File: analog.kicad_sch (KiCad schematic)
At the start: 62 parts, among them J8 Sensor harness, J9 Spare diff in, U6 ADS1115 (0x48), U7 ADS1115 (0x49)

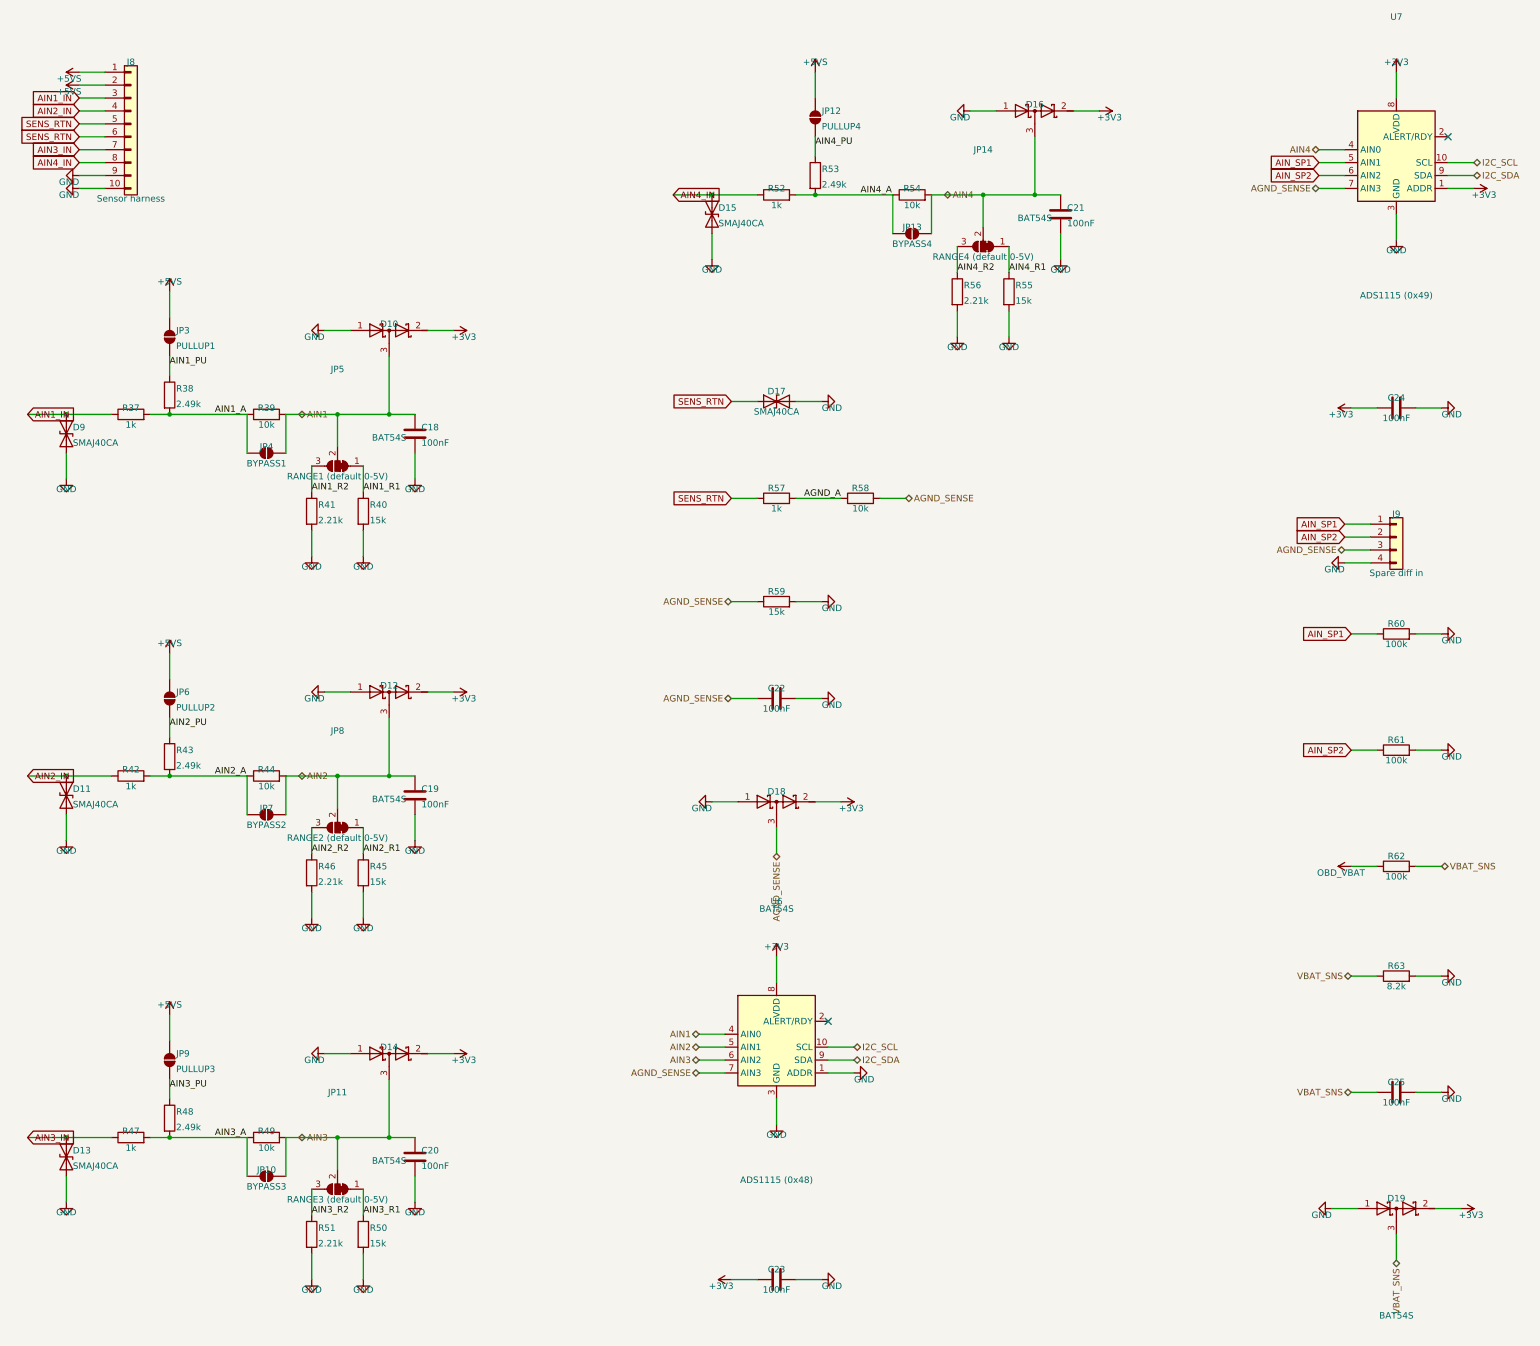
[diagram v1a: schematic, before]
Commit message: Second CAN bus, single analog range, and three placement bugs the render caught
TWO CAN BUSES AT ONCE NEEDS A SECOND CONTROLLER. The ESP32-S3 has exactly
one TWAI peripheral. Two transceivers on it would give a bus you can pick at
runtime through the GPIO matrix, never two live at once, and the point of a
second bus is watching the powertrain and the body bus together. So the
second channel is an MCP2518FD on SPI (SOIC-14, KiCad ships the pin-compatible
MCP2517FD symbol) with its own 40 MHz crystal, its own TJA1051 -- same part
as CAN 1, so two positions on one BOM line -- choke, split termination and
clamps.

That cost five pins against two spare. The three came from dropping the
microSD to 1-bit SDMMC, which measurement says is free: the busiest case this
logger will see is ~128 kB/s against 1-bit's ~1500 kB/s, and bus width does
not touch the card's internal write stall, which is the only thing the
hold-up budget is actually sized around. The card keeps its D1/D2/D3
pull-ups because a card samples DAT3 at power-up and drops into SPI mode if
it finds it low -- they simply stop at the socket now.

Jumpers on the aux harness pins pick K-line or the second CAN pair, because
those two genuinely cannot share a wire: K-line idles at battery voltage and
a CAN transceiver biases its bus to 2.5 V. The clamps sit ahead of the
jumpers so the protection is the same either way, which also let the K-line
drop its own TVS. Default is K-line, which is what an R53 wants.

ANALOG DOWN TO ONE RANGE. The bypass and range-select jumpers are gone --
twelve jumpers and four resistors -- and every channel is a fixed 2.21/13.21
divider spanning 0-16 V, so a 5 V and a 12 V sensor both fit without
touching anything. Resolution was never the reason for a narrower range: a
5 V sensor lands at 0.836 V, which on a 16-bit ADS1115 is 6688 counts.

The real reason is the differential ground. A channel switched to 0-16 V
while the shared return attenuator stayed at the 0-5 V ratio subtracts
0.5769*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
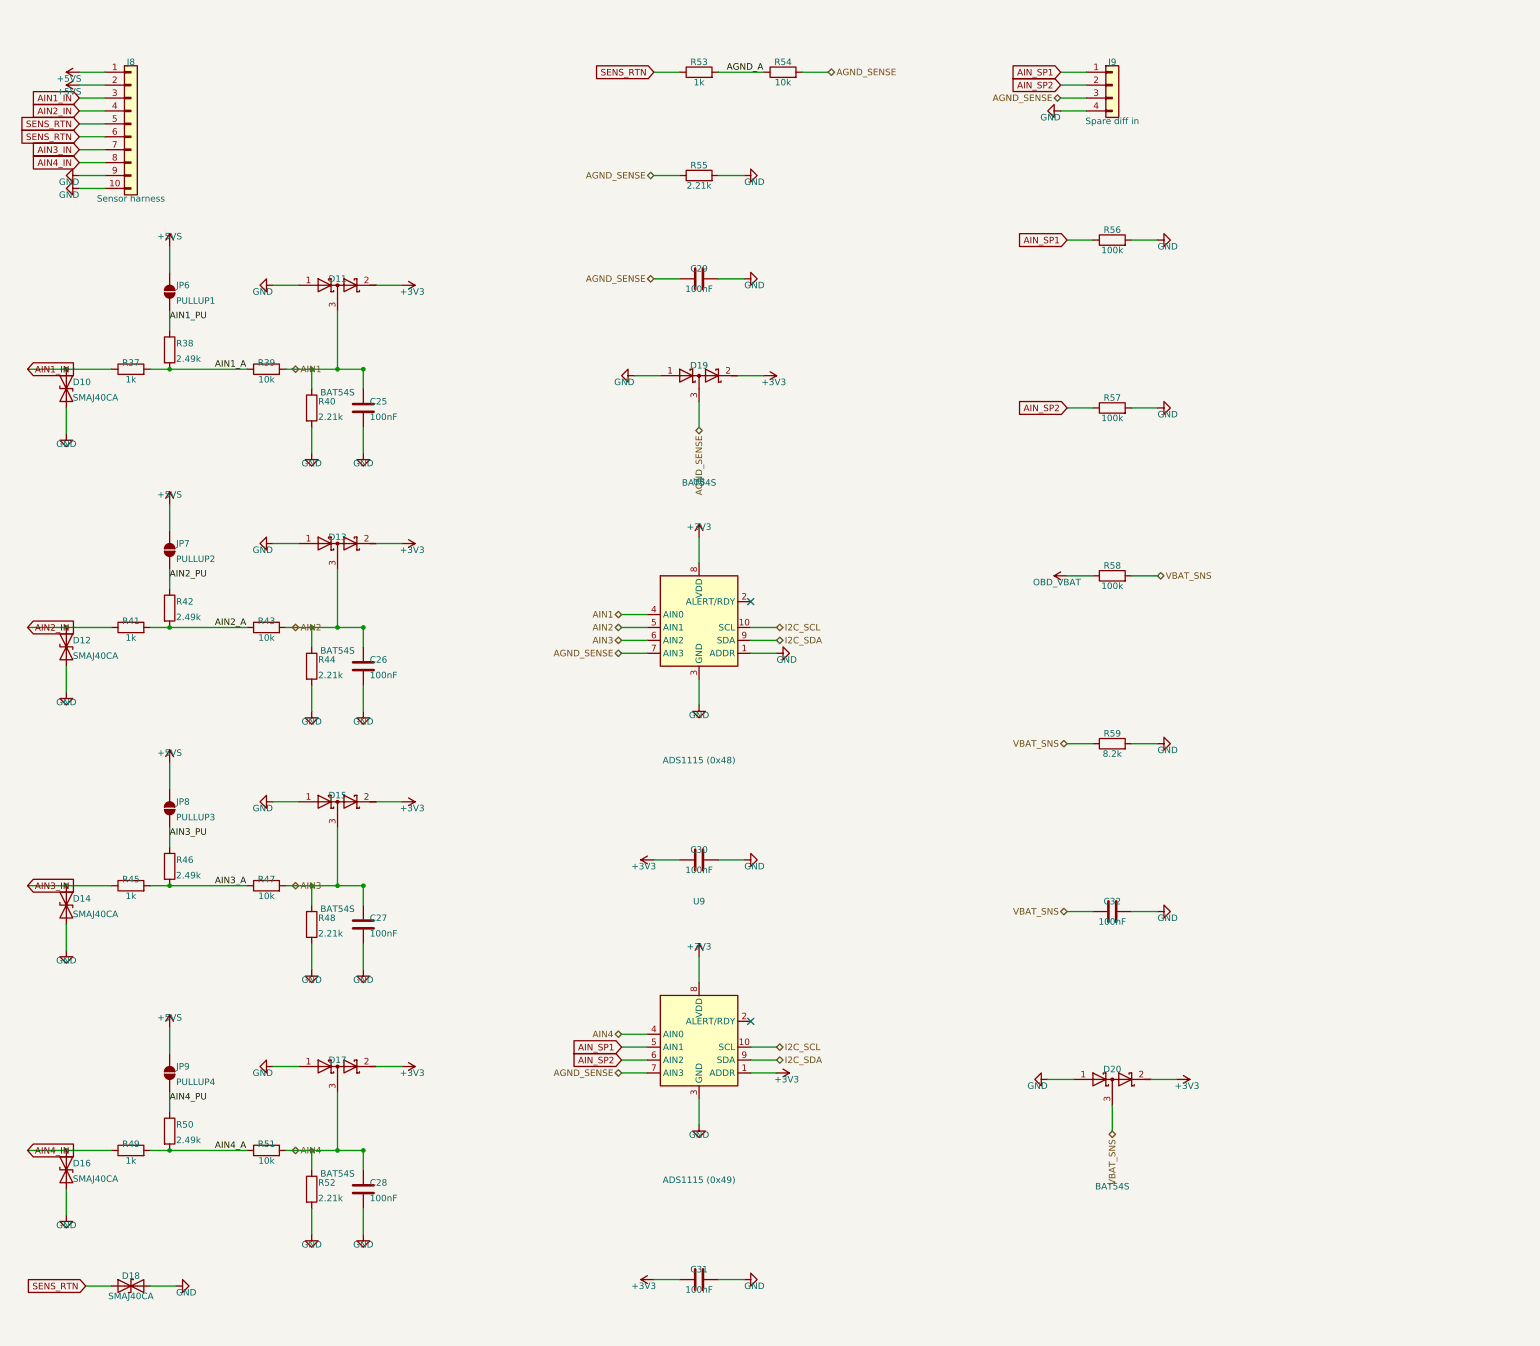
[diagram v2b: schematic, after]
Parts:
- removed C18, C19, C20, C21, C22, C23, C24: 100nF, Capacitor_SMD:C_0805_2012Metric, symbol Device:C
- removed D9: SMAJ40CA, Diode_SMD:D_SMA, symbol Device:D_TVS
- removed JP10: BYPASS3, Jumper:SolderJumper-2_P1.3mm_Open_Pad1.0x1.5mm, symbol Jumper:SolderJumper_2_Open
- removed JP11: RANGE3 (default 0-5V), Jumper:SolderJumper-3_P1.3mm_Bridged12_Pad1.0x1.5mm, symbol Jumper:SolderJumper_3_Bridged12
- removed JP12: PULLUP4, Jumper:SolderJumper-2_P1.3mm_Open_Pad1.0x1.5mm, symbol Jumper:SolderJumper_2_Open
- removed JP13: BYPASS4, Jumper:SolderJumper-2_P1.3mm_Open_Pad1.0x1.5mm, symbol Jumper:SolderJumper_2_Open
- removed JP14: RANGE4 (default 0-5V), Jumper:SolderJumper-3_P1.3mm_Bridged12_Pad1.0x1.5mm, symbol Jumper:SolderJumper_3_Bridged12
- removed JP3: PULLUP1, Jumper:SolderJumper-2_P1.3mm_Open_Pad1.0x1.5mm, symbol Jumper:SolderJumper_2_Open
- removed JP4: BYPASS1, Jumper:SolderJumper-2_P1.3mm_Open_Pad1.0x1.5mm, symbol Jumper:SolderJumper_2_Open
- removed JP5: RANGE1 (default 0-5V), Jumper:SolderJumper-3_P1.3mm_Bridged12_Pad1.0x1.5mm, symbol Jumper:SolderJumper_3_Bridged12
- removed R60, R61, R62: 100k, Resistor_SMD:R_0805_2012Metric, symbol Device:R
- removed R63: 8.2k, Resistor_SMD:R_0805_2012Metric, symbol Device:R
- removed U6: ADS1115 (0x48), Package_SO:VSSOP-10_3x3mm_P0.5mm, symbol Analog_ADC:ADS1115IDGS
- removed U7: ADS1115 (0x49), Package_SO:VSSOP-10_3x3mm_P0.5mm, symbol Analog_ADC:ADS1115IDGS
- added C26, C27, C28, C29, C30, C31, C32: 100nF, Capacitor_SMD:C_0805_2012Metric, symbol Device:C
- added D20: BAT54S, Package_TO_SOT_SMD:SOT-23, symbol Device:D_Schottky_Dual_Series_AKC
- added U8: ADS1115 (0x48), Package_SO:VSSOP-10_3x3mm_P0.5mm, symbol Analog_ADC:ADS1115IDGS
- added U9: ADS1115 (0x49), Package_SO:VSSOP-10_3x3mm_P0.5mm, symbol Analog_ADC:ADS1115IDGS
- C25: Note (none) -> Ch1 anti-alias / ADC charge reservoir
- D10: value BAT54S -> SMAJ40CA; footprint Package_TO_SOT_SMD:SOT-23 -> Diode_SMD:D_SMA; symbol Device:D_Schottky_Dual_Series_AKC -> Device:D_TVS; MPN MDD BAT54S -> Littelfuse SMAJ40CA; Note Ch1 rail clamp (both polarities) -> Ch1 harness transient clamp (bidirectional, 400W)
- D11: value SMAJ40CA -> BAT54S; footprint Diode_SMD:D_SMA -> Package_TO_SOT_SMD:SOT-23; symbol Device:D_TVS -> Device:D_Schottky_Dual_Series_AKC; MPN Littelfuse SMAJ40CA -> MDD BAT54S; Note Ch2 harness transient clamp (bidirectional, 400W) -> Ch1 rail clamp (both polarities)
- D12: value BAT54S -> SMAJ40CA; footprint Package_TO_SOT_SMD:SOT-23 -> Diode_SMD:D_SMA; symbol Device:D_Schottky_Dual_Series_AKC -> Device:D_TVS; MPN MDD BAT54S -> Littelfuse SMAJ40CA; Note Ch2 rail clamp (both polarities) -> Ch2 harness transient clamp (bidirectional, 400W)
- D13: value SMAJ40CA -> BAT54S; footprint Diode_SMD:D_SMA -> Package_TO_SOT_SMD:SOT-23; symbol Device:D_TVS -> Device:D_Schottky_Dual_Series_AKC; MPN Littelfuse SMAJ40CA -> MDD BAT54S; Note Ch3 harness transient clamp (bidirectional, 400W) -> Ch2 rail clamp (both polarities)
- D14: value BAT54S -> SMAJ40CA; footprint Package_TO_SOT_SMD:SOT-23 -> Diode_SMD:D_SMA; symbol Device:D_Schottky_Dual_Series_AKC -> Device:D_TVS; MPN MDD BAT54S -> Littelfuse SMAJ40CA; Note Ch3 rail clamp (both polarities) -> Ch3 harness transient clamp (bidirectional, 400W)
- D15: value SMAJ40CA -> BAT54S; footprint Diode_SMD:D_SMA -> Package_TO_SOT_SMD:SOT-23; symbol Device:D_TVS -> Device:D_Schottky_Dual_Series_AKC; MPN Littelfuse SMAJ40CA -> MDD BAT54S; Note Ch4 harness transient clamp (bidirectional, 400W) -> Ch3 rail clamp (both polarities)
- D16: value BAT54S -> SMAJ40CA; footprint Package_TO_SOT_SMD:SOT-23 -> Diode_SMD:D_SMA; symbol Device:D_Schottky_Dual_Series_AKC -> Device:D_TVS; MPN MDD BAT54S -> Littelfuse SMAJ40CA; Note Ch4 rail clamp (both polarities) -> Ch4 harness transient clamp (bidirectional, 400W)
- D17: value SMAJ40CA -> BAT54S; footprint Diode_SMD:D_SMA -> Package_TO_SOT_SMD:SOT-23; symbol Device:D_TVS -> Device:D_Schottky_Dual_Series_AKC; MPN Littelfuse SMAJ40CA -> MDD BAT54S; Note Return-sense harness clamp. This wire is as exposed as the 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 -> Ch4 rail clamp (both polarities)
- D18: value BAT54S -> SMAJ40CA; footprint Package_TO_SOT_SMD:SOT-23 -> Diode_SMD:D_SMA; symbol Device:D_Schottky_Dual_Series_AKC -> Device:D_TVS; MPN MDD BAT54S -> Littelfuse SMAJ40CA; Note Return-sense rail clamp. +/-0.5 V of chassis offset arrives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 -> Return-sense harness clamp. This wire is as exposed as the 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
- D19: Note Battery-monitor clamp -> Return-sense rail clamp. +/-0.5 V of chassis offset arrives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
- JP6: value PULLUP2 -> PULLUP1; Note Close for 2-wire NTC / open-collector sensors -> Close for 2-wire NTC / open-collector sensors. Nothing to d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
- JP7: value BYPASS2 -> PULLUP2; Note Close for a raw 0-3.3V sensor (shorts the upper leg) -> Close for 2-wire NTC / open-collector sensors. Nothing to d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
- JP8: value RANGE2 (default 0-5V) -> PULLUP3; footprint Jumper:SolderJumper-3_P1.3mm_Bridged12_Pad1.0x1.5mm -> Jumper:SolderJumper-2_P1.3mm_Open_Pad1.0x1.5mm; symbol Jumper:SolderJumper_3_Bridged12 -> Jumper:SolderJumper_2_Open; Note Ships BRIDGED 1-2 = the 0-5V range, which is what almost ev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 -> Close for 2-wire NTC / open-collector sensors. Nothing to d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
- JP9: value PULLUP3 -> PULLUP4; Note Close for 2-wire NTC / open-collector sensors -> Close for 2-wire NTC / open-collector sensors. Nothing to d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
- R40: value 15k -> 2.21k; Note 0-5V range: 5.0V in -> ~2.88V at the ADC (1k series include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 -> Ch1 divider lower leg. 2.21/13.21 = 0.1673, so 16.0 V in gi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
- R41: value 2.21k -> 1k; Note 0-16V range: 16.0V in -> ~2.67V at the ADC (1k series inclu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 -> Ch2 series/fault-current limit; 0.1% thin film -- it is ins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
- R42: value 1k -> 2.49k; Note Ch2 series/fault-current limit; 0.1% thin film -- it is ins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 -> Ch2 bias resistor; Tolerance 0.1% -> (none)
- R43: value 2.49k -> 10k; Note Ch2 bias resistor -> Ch2 divider upper leg, 0.1% thin film for AFR-grade accuracy; Tolerance (none) -> 0.1%
- R44: value 10k -> 2.21k; Note Ch2 divider upper leg, 0.1% thin film for AFR-grade accuracy -> Ch2 divider lower leg. 2.21/13.21 = 0.1673, so 16.0 V in gi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
- R45: value 15k -> 1k; Note 0-5V range: 5.0V in -> ~2.88V at the ADC (1k series include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 -> Ch3 series/fault-current limit; 0.1% thin film -- it is ins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
- R46: value 2.21k -> 2.49k; Note 0-16V range: 16.0V in -> ~2.67V at the ADC (1k series inclu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 -> Ch3 bias resistor; Tolerance 0.1% -> (none)
- R47: value 1k -> 10k; Note Ch3 series/fault-current limit; 0.1% thin film -- it is ins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 -> Ch3 divider upper leg, 0.1% thin film for AFR-grade accuracy
- R48: value 2.49k -> 2.21k; Note Ch3 bias resistor -> Ch3 divider lower leg. 2.21/13.21 = 0.1673, so 16.0 V in gi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; Tolerance (none) -> 0.1%
- R49: value 10k -> 1k; Note Ch3 divider upper leg, 0.1% thin film for AFR-grade accuracy -> Ch4 series/fault-current limit; 0.1% thin film -- it is ins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
- R50: value 15k -> 2.49k; Note 0-5V range: 5.0V in -> ~2.88V at the ADC (1k series include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 -> Ch4 bias resistor; Tolerance 0.1% -> (none)
- R51: value 2.21k -> 10k; Note 0-16V range: 16.0V in -> ~2.67V at the ADC (1k series inclu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 -> Ch4 divider upper leg, 0.1% thin film for AFR-grade accuracy
- R52: value 1k -> 2.21k; Note Ch4 series/fault-current limit; 0.1% thin film -- it is ins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 -> Ch4 divider lower leg. 2.21/13.21 = 0.1673, so 16.0 V in gi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
- R53: value 2.49k -> 1k; Note Ch4 bias resistor -> Matches the channels' 1k series; Tolerance (none) -> 0.1%
- R54: Note Ch4 divider upper leg, 0.1% thin film for AFR-grade accuracy -> Matches the channels' upper leg
- R55: value 15k -> 2.21k; Note 0-5V range: 5.0V in -> ~2.88V at the ADC (1k series include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 -> Matches the channels' lower leg. Same value, same 0.1%% par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
- R56: value 2.21k -> 100k; Note 0-16V range: 16.0V in -> ~2.67V at the ADC (1k series inclu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 -> Bleed: an open input is not a reading; Tolerance 0.1% -> (none)
- R57: value 1k -> 100k; Note Matches the channels' 1k series -> (none); Tolerance 0.1% -> (none)
- R58: value 10k -> 100k; Note Matches the channels' upper leg -> Battery monitor, upper leg; Tolerance 0.1% -> (none)
- R59: value 15k -> 8.2k; Note Matches the channels' 0-5V lower leg. Also what holds AGND_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 -> Divide by 13.2, not 11: at 36V the 11:1 divider put 3.27V o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; Tolerance 0.1% -> (none)
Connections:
- net AIN1_R1 is gone; now on net AIN1: R40.1
- net AIN1_R2 is gone; now on net AIN2_IN: R41.1
- net AIN3_R1 is gone; now on net AIN4_PU: R50.1
- net AIN3_R2 is gone; now on net AIN4_A: R51.1
- net AIN4_R1 is gone; now on net AGND_SENSE: R55.1
- net AIN4_R2 is gone; now on net AIN_SP1: R56.1
- net +3V3: now also D11.2 (K), D13.2 (K), D15.2 (K), D17.2 (K), C30.1, C31.1, D20.2 (K), U8.8 (VDD), U9.1 (ADDR), U9.8 (VDD); no longer D10.2 (K), D12.2 (K), D14.2 (K), D16.2 (K), D18.2 (K)
- net +5VS: now also JP7.1 (A), JP8.1 (A)
- net AGND_A: now also R53.2, R54.1; no longer R57.2, R58.1
- net AGND_SENSE: now also D19.3 (common), R54.2, C29.1, U8.7 (AIN3), U9.7 (AIN3); no longer D18.3 (common), R58.2, R59.1
- net AIN1: now also C25.1, D11.3 (common), U8.4 (AIN0); no longer D10.3 (common)
- net AIN1_IN: now also D10.1 (A1)
- net AIN1_PU: now also JP6.2 (B)
- net AIN2: now also D13.3 (common), R43.2, R44.1, C26.1, U8.5 (AIN1); no longer D12.3 (common), JP7.2 (B), JP8.2 (C), R44.2
- net AIN2_A: now also R41.2, R43.1; no longer JP7.1 (A), R43.2, R44.1
- net AIN2_IN: now also D12.1 (A1); no longer D11.1 (A1), R42.1
- net AIN2_PU: now also JP7.2 (B), R42.1; no longer JP6.2 (B), R43.1
- net AIN3: now also D15.3 (common), R47.2, R48.1, C27.1, U8.6 (AIN2); no longer D14.3 (common), R49.2
- net AIN3_A: now also R45.2, R46.2, R47.1; no longer R47.2, R48.2, R49.1
- net AIN3_IN: now also D14.1 (A1), R45.1; no longer D13.1 (A1), R47.1
- net AIN3_PU: now also JP8.2 (B), R46.1; no longer JP9.2 (B), R48.1
- net AIN4: now also D17.3 (common), R51.2, R52.1, C28.1, U9.4 (AIN0); no longer D16.3 (common), R54.2
- net AIN4_A: now also R49.2, R50.2; no longer R52.2, R53.2, R54.1
- net AIN4_IN: now also D16.1 (A1), R49.1; no longer D15.1 (A1), R52.1
- net AIN4_PU: now also JP9.2 (B); no longer R53.1
- net AIN_SP1: now also U9.5 (AIN1)
- net AIN_SP2: now also R57.1, U9.6 (AIN2)
- net GND: now also D10.2 (A2), D11.1 (A), D12.2 (A2), D13.1 (A), D14.2 (A2), D15.1 (A), D16.2 (A2), D17.1 (A), D18.2 (A2), R44.2, R48.2, R52.2, R57.2, C26.2, C27.2, C28.2, C29.2, C30.2, C31.2, C32.2, D20.1 (A), U8.1 (ADDR), U8.3 (GND), U9.3 (GND); no longer D10.1 (A), D11.2 (A2), D12.1 (A), D13.2 (A2), D14.1 (A), D15.2 (A2), D16.1 (A), D17.2 (A2), D18.1 (A), R41.2, R45.2, R46.2, R50.2, R51.2
- net I2C_SCL: now also U8.10 (SCL), U9.10 (SCL)
- net I2C_SDA: now also U8.9 (SDA), U9.9 (SDA)
- net OBD_VBAT: now also R58.1
- net SENS_RTN: now also D18.1 (A1), R53.1; no longer D17.1 (A1), R57.1
- net VBAT_SNS: now also R58.2, R59.1, C32.1, D20.3 (common); no longer C25.1, D19.3 (common)
- removed net AIN2_R1: JP8.1 (A), R45.1
- removed net AIN2_R2: JP8.3 (B), R46.1
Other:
- moved on the sheet: C25, D19, J9, JP6, JP7, JP9, R37, R38, R39, R40, R41, R42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
